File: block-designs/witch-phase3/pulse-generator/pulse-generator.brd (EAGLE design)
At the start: 159.8 x 99.1 mm, 91 parts, among them IC1 74LVC1G17DBV, IC10 74LVC1G08DBV, IC11 74LVC1G08DBV, IC12 741G175, IC13 741G175, IC14 741G175, IC15 741G175, IC16 741G175, IC17 74LVC1G04DBV, IC18 74LVC1G04DBV, IC19 74LVC1G08DBV, IC2 74LVC1G17DBV, IC20 74LVC1G04DBV, IC21 74LVC1G08DBV, IC22 741G175, IC23 74LVC1G08DBV, IC3 74LVC1G17DBV, IC4 NE555D, IC5 741G175, IC6 74LVC1G04DBV, IC7 74LVC1G04DBV, IC8 741G175, IC9 741G175, J1 POWER_JACKPTH, Q1 MMBT2222A, Q2 MMBT2222A, Q3 MMBT2222A, Q4 MMBT2222A, Q5 MMBT2222A, Q6 MMBT2907ALT1SMD

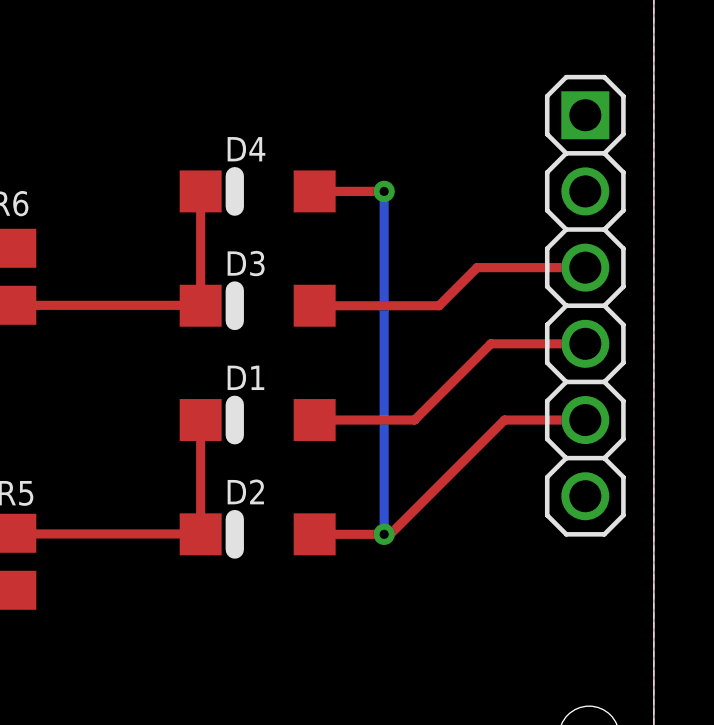
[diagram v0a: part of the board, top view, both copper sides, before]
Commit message: update schematic and layout for off-by-one error on add/comp clr singals
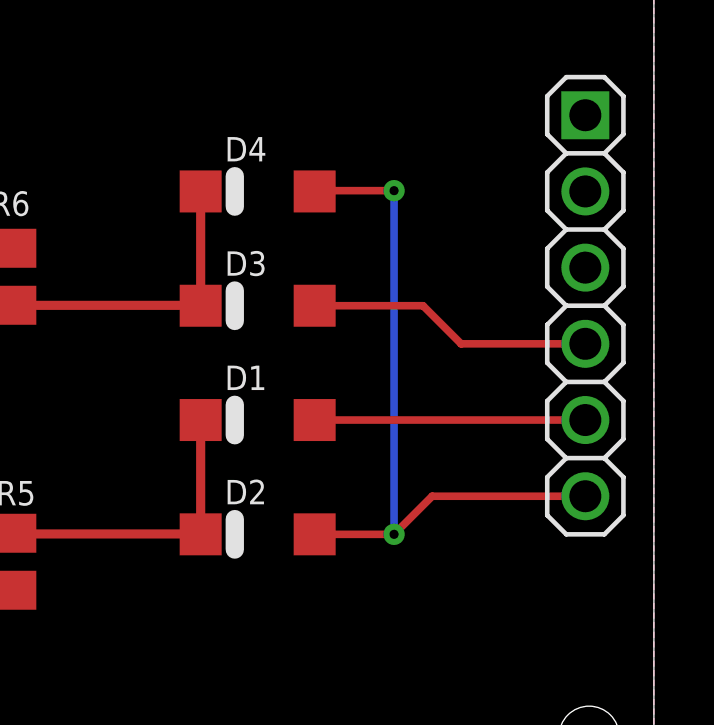
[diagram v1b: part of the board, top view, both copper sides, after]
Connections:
- net FOUR: now also D2.A, D4.A
- net ONE: no longer D3.A
- net THREE: now also D1.A; no longer D2.A, D4.A
- net TWO: now also D3.A; no longer D1.A
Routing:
- net FOUR: track 0.00 -> 23.7 mm, vias 0 -> 2
- net THREE: track 24.3 -> 9.02 mm, vias 2 -> 0
- net ONE: track 9.55 -> 0.00 mm
- net TWO: track 10.1 -> 9.55 mm
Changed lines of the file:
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@@
 </signal>
 <signal name="ONE">
-<contactref element="D3" pad="A"/>
 <contactref element="JP5" pad="3"/>
-<wire x1="157.48" y1="17.78" x2="153.8732" y2="17.78" width="0.3048" layer="1"/>
-<wire x1="153.8732" y1="17.78" x2="152.6032" y2="16.51" width="0.3048" layer="1"/>
-<wire x1="152.6032" y1="16.51" x2="148.458" y2="16.51" width="0.3048" layer="1"/>
 </signal>
 <signal name="TWO">
-<contactref element="D1" pad="A"/>
 <contactref element="JP5" pad="4"/>
-<wire x1="157.48" y1="15.24" x2="154.3304" y2="15.24" width="0.3048" layer="1"/>
-<wire x1="154.3304" y1="15.24" x2="151.7904" y2="12.7" width="0.3048" layer="1"/>
-<wire x1="151.7904" y1="12.7" x2="148.458" y2="12.7" width="0.3048" layer="1"/>
+<contactref element="D3" pad="A"/>
+<wire x1="157.48" y1="15.24" x2="153.3398" y2="15.24" width="0.254" layer="1"/>
+<wire x1="153.3398" y1="15.24" x2="152.0698" y2="16.51" width="0.254" layer="1"/>
+<wire x1="152.0698" y1="16.51" x2="148.458" y2="16.51" width="0.254" layer="1"/>
 </signal>
 <signal name="N$18">
@@
 </signal>
 <signal name="THREE">
-<contactref element="D4" pad="A"/>
-<contactref element="D2" pad="A"/>
 <contactref element="JP5" pad="5"/>
-<wire x1="157.48" y1="12.7" x2="154.7876" y2="12.7" width="0.3048" layer="1"/>
-<wire x1="154.7876" y1="12.7" x2="150.9776" y2="8.89" width="0.3048" layer="1"/>
-<wire x1="150.9776" y1="8.89" x2="150.7744" y2="8.89" width="0.3048" layer="1"/>
-<wire x1="150.7744" y1="8.89" x2="148.458" y2="8.89" width="0.3048" layer="1"/>
-<wire x1="148.458" y1="20.32" x2="150.7744" y2="20.32" width="0.3048" layer="1"/>
-<via x="150.7744" y="20.32" extent="1-16" drill="0.3048"/>
-<wire x1="150.7744" y1="20.32" x2="150.7744" y2="8.89" width="0.3048" layer="16"/>
-<via x="150.7744" y="8.89" extent="1-16" drill="0.3048"/>
+<contactref element="D1" pad="A"/>
+<wire x1="157.48" y1="12.7" x2="148.458" y2="12.7" width="0.254" layer="1"/>
 </signal>
 <signal name="FOUR">
 <contactref element="JP5" pad="6"/>
+<contactref element="D2" pad="A"/>
+<contactref element="D4" pad="A"/>
+<wire x1="148.458" y1="20.32" x2="148.4834" y2="20.3454" width="0.254" layer="1"/>
+<wire x1="148.4834" y1="20.3454" x2="151.1046" y2="20.3454" width="0.254" layer="1"/>
+<via x="151.1046" y="20.3454" extent="1-16" drill="0.3048"/>
+<wire x1="151.1046" y1="20.3454" x2="151.1046" y2="8.89" width="0.254" layer="16"/>
+<via x="151.1046" y="8.89" extent="1-16" drill="0.3048"/>
+<wire x1="151.1046" y1="8.89" x2="148.458" y2="8.89" width="0.254" layer="1"/>
+<wire x1="157.48" y1="10.16" x2="152.3746" y2="10.16" width="0.254" layer="1"/>
+<wire x1="152.3746" y1="10.16" x2="151.1046" y2="8.89" width="0.254" layer="1"/>
 </signal>
 <signal name="ZERO">

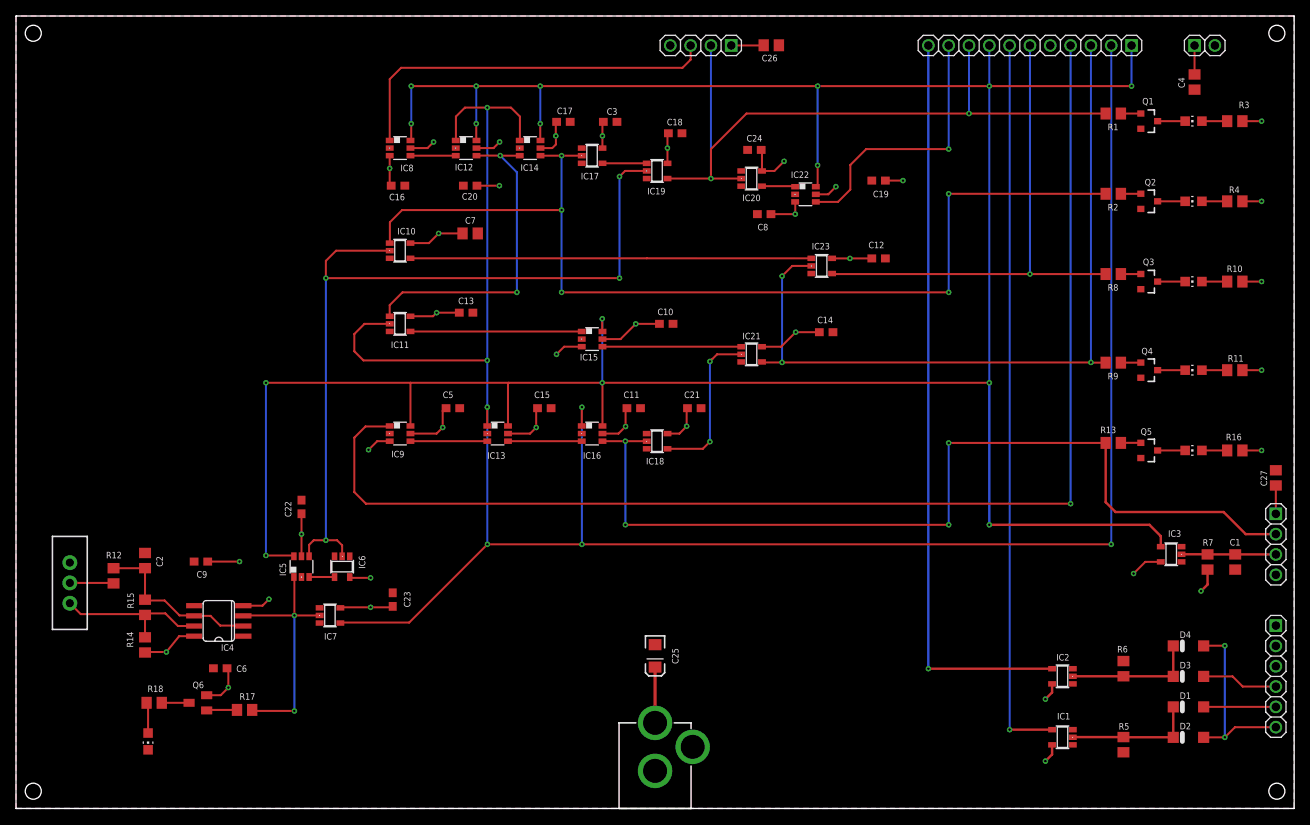
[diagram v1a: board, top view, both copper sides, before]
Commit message: add function select LEDs
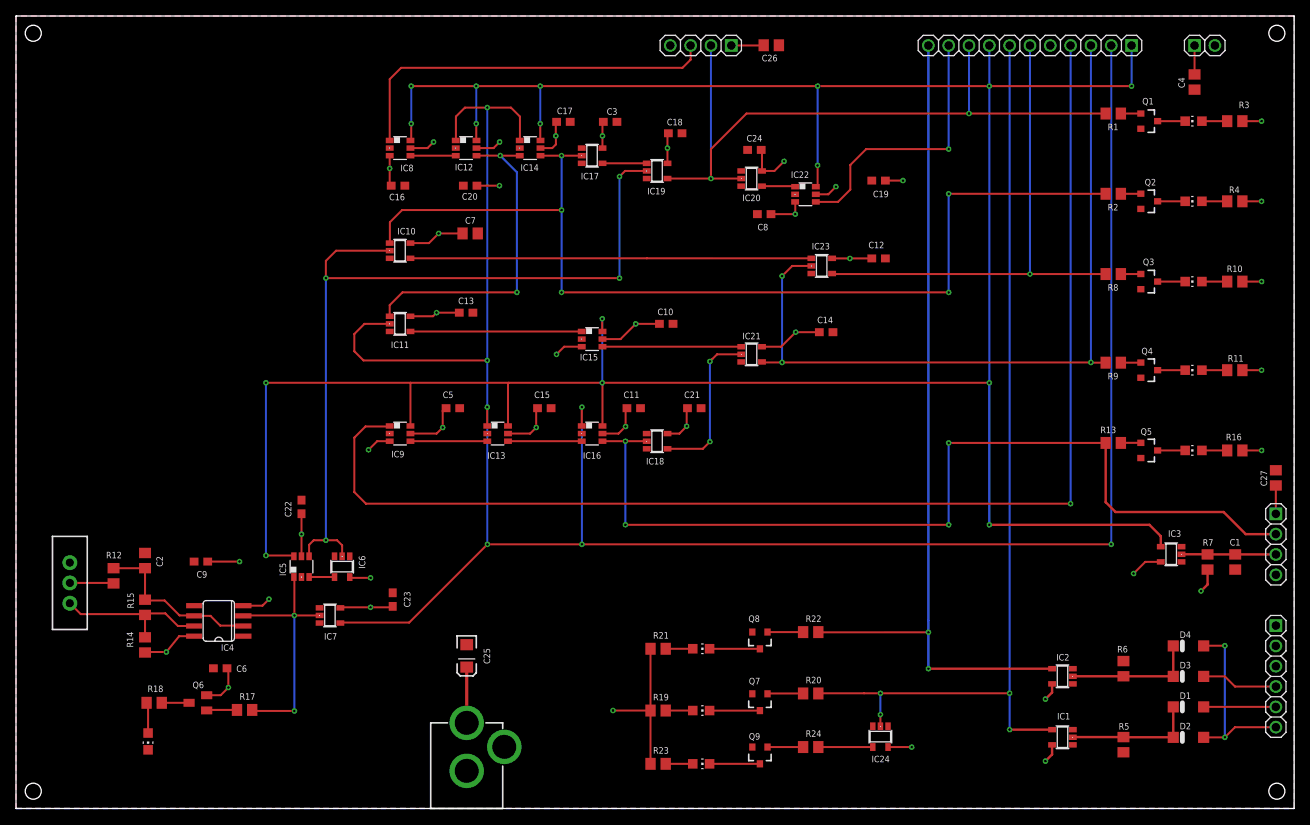
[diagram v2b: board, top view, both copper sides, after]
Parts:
- added IC24: 74LVC1G04DBV, 74xx-little-us:SOT23-5
- added LED7, LED8, LED9: (no value), led:CHIP-LED0805
- added Q7, Q8, Q9: MMBT2222A, SparkFun-DiscreteSemi:SOT23-3
- added R19, R21, R23: 270, resistor:R0805
- added R20, R22, R24: 1K, resistor:R0805
- moved C25 23.5 mm to (56.3, 19.1)
- moved J1 23.5 mm to (56.3, -3.00)
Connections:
- new net N$12: LED7.C, Q7.3
- new net N$14: Q7.1, R20.1
- new net N$20: LED7.A, R19.2
- new net N$21: LED8.C, Q8.3
- new net N$22: Q8.1, R22.1
- new net N$27: LED8.A, R21.2
- new net N$29: LED9.C, Q9.3
- new net N$30: Q9.1, R24.1
- new net N$40: LED9.A, R23.2
- new net N$41: IC24.4, R24.2
- net ADD/COMP: now also IC24.2, R20.2
- net CLR: now also R22.2
- net GND: now also IC24.3, Q7.2, Q8.2, Q9.2
- net VCC: now also IC24.5, R19.1, R21.1, R23.1
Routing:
- net ADD/COMP: track 90.8 -> 118.9 mm, vias 1 -> 4
- net VCC: track 182.4 -> 204.5 mm, vias 38 -> 40
- net CLR: track 93.4 -> 107.1 mm, vias 1 -> 2
- net N$41: track 0.00 -> 6.81 mm
- net N$21: track 0.00 -> 6.29 mm
- net N$12: track 0.00 -> 6.29 mm
- net N$29: track 0.00 -> 6.29 mm
- net N$14: track 0.00 -> 4.47 mm
- net N$22: track 0.00 -> 4.45 mm
- net N$30: track 0.00 -> 4.45 mm
- net N$40: track 0.00 -> 3.38 mm
- net N$27: track 0.00 -> 3.38 mm
- net N$20: track 0.00 -> 3.38 mm
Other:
- board text added: "ADD"
- board text added: "CLR"
- board text added: "SUB"

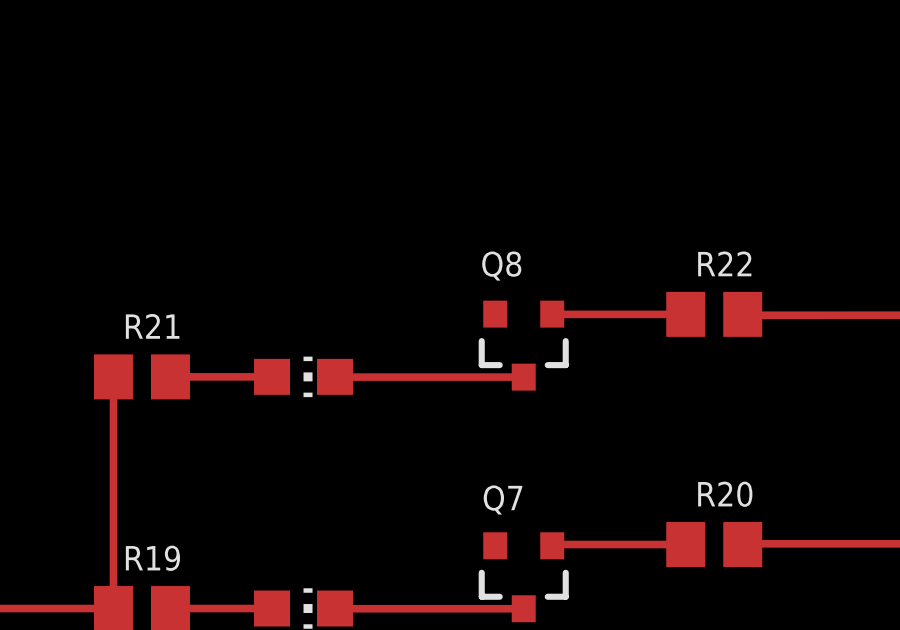
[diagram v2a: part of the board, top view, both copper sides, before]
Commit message: add LEDs for functions and tweak layout
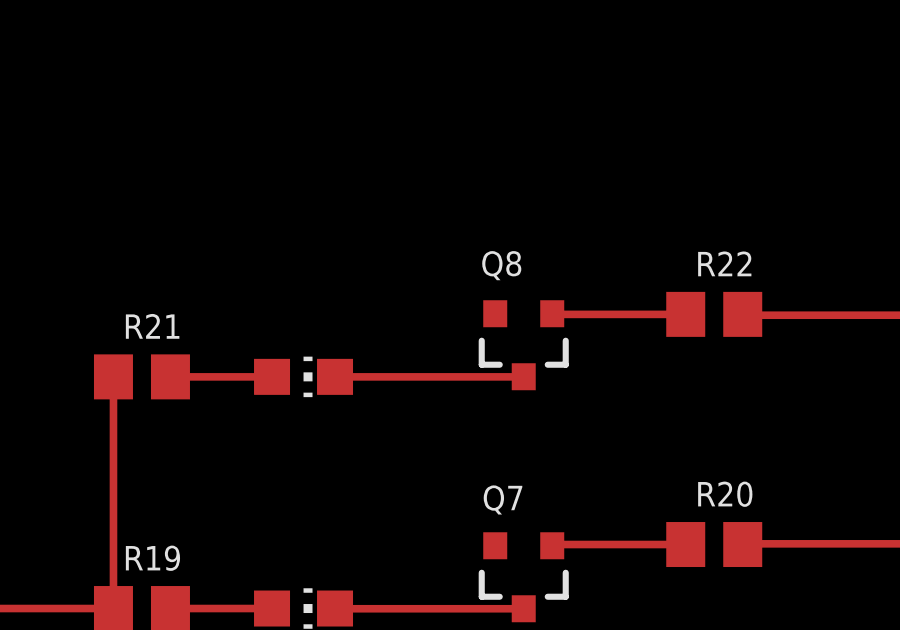
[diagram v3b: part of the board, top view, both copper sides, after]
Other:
- board text added: "Revision 3"
- board text removed: "Revision 2"
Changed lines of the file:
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@@
 <text x="147.193" y="72.7202" size="1.778" layer="48" align="center">TDONE</text>
 <text x="147.193" y="41.656" size="1.778" layer="48" align="center">CDONE</text>
-<text x="6.35" y="78.3336" size="0.8128" layer="48">Revision 2</text>
+<text x="6.35" y="78.3336" size="0.8128" layer="48">Revision 3</text>
 <text x="85.6488" y="22.0472" size="1.778" layer="48" align="center">CLR</text>
 <text x="85.6488" y="14.3256" size="1.778" layer="48" align="center">SUB</text>
@@
 <attribute name="VALUE" x="98.7044" y="19.5072" size="1.27" layer="27"/>
 </element>
-<element name="Q8" library="SparkFun-DiscreteSemi" package="SOT23-3" value="MMBT2222A" x="92.9894" y="21.0566" smashed="yes" rot="R180">
-<attribute name="PROD_ID" value="TRANS-08049" x="102.0318" y="17.145" size="1.778" layer="27" rot="R180" display="off"/>
-<attribute name="NAME" x="92.9767" y="24.13" size="0.8128" layer="25" rot="R180"/>
-<attribute name="VALUE" x="94.0054" y="21.2471" size="0.4064" layer="27" rot="R180"/>
+<element name="Q8" library="SparkFun-DiscreteSemi" package="SOT23-3" value="MMBT2222A" x="92.9894" y="21.0693" smashed="yes" rot="R180">
+<attribute name="PROD_ID" value="TRANS-08049" x="102.0318" y="17.1577" size="1.778" layer="27" rot="R180" display="off"/>
+<attribute name="NAME" x="92.9767" y="24.1427" size="0.8128" layer="25" rot="R180"/>
+<attribute name="VALUE" x="94.0054" y="21.2598" size="0.4064" layer="27" rot="R180"/>
 </element>
 <element name="LED9" library="led" package="CHIP-LED0805" value="" x="85.6488" y="5.5802" smashed="yes" rot="R270">
@@
 <contactref element="Q8" pad="3"/>
 <contactref element="LED8" pad="C"/>
-<wire x1="92.9894" y1="19.9566" x2="86.7066" y2="19.9566" width="0.254" layer="1"/>
-<wire x1="86.7066" y1="19.9566" x2="86.6988" y2="19.9644" width="0.254" layer="1"/>
+<wire x1="86.6988" y1="19.9644" x2="92.9845" y2="19.9644" width="0.254" layer="1"/>
+<wire x1="92.9845" y1="19.9644" x2="92.9894" y2="19.9693" width="0.254" layer="1"/>
 </signal>
 <signal name="N$22">
@@
 <contactref element="R22" pad="1"/>
 <wire x1="98.3894" y1="22.0472" x2="93.9488" y2="22.0472" width="0.254" layer="1"/>
-<wire x1="93.9488" y1="22.0472" x2="93.9394" y2="22.0566" width="0.254" layer="1"/>
+<wire x1="93.9488" y1="22.0472" x2="93.9394" y2="22.0693" width="0.254" layer="1"/>
 </signal>
 <signal name="N$27">
